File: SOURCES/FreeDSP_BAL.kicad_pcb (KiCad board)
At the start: 2 copper layers, 100 x 100 mm, 187 parts, among them IC1 AD8608ARZ, IC2 ADAU1701, IC3 24AA256, IC4 SN74LVC1G08DBVR, IC5 AD8608ARZ, IC6 AD8608ARZ, IC7 74HC4040D, P10 CONN_02X10, P11 MM-16G, P12 MM-12G, P2 BARREL_JACK, P3 CONN_02X02, P4 USBi, P5 CONN_02X13, P6 CONN_01X06, P7 CONN_01X06, P8 CONN_01X06, P9 CONN_02X10, Q1 ZXTP25040DFHTA, Q2 2N7000, Q3 2N7000, U1 78033, U3 7805

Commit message: Correction of some typos
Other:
- board text added: "12V->exp"
- board text removed: "exp 5V"
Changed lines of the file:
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@@
     (links 416)
     (no_connects 0)
-    (area 99.949999 49.949999 200.050001 150.050001)
+    (area 93.224999 49.949999 202.475621 150.050001)
     (thickness 1.6)
     (drawings 13)
@@
     (pad 17 thru_hole circle (at 8.385 0.53 270) (size 1.5 1.5) (drill 1.5) (layers *.Cu *.Mask F.SilkS))
   )
-  (gr_text "Designed in Germany" (at 168.9 147.3) (layer F.SilkS)
+  (gr_text "Designed in Germany" (at 150.2 134.6 90) (layer F.SilkS)
     (effects (font (size 1.5 1.5) (thickness 0.3)))
   )
-  (gr_text freeDSP-CLASSIC-BAL-A (at 193 124 90) (layer F.SilkS)
+  (gr_text freeDSP-CLASSIC-BAL-A (at 147.5 132 90) (layer F.SilkS)
     (effects (font (size 1.5 1.5) (thickness 0.3)))
   )
@@
   (gr_line (start 100 50) (end 200 50) (layer Edge.Cuts) (width 0.1))
   (gr_line (start 100 150) (end 100 50) (layer Edge.Cuts) (width 0.1))
-  (gr_text "exp 5V" (at 184.5 76.5 90) (layer F.SilkS)
+  (gr_text 12V->exp (at 184.1 77.9 90) (layer F.SilkS)
     (effects (font (size 1.5 1.5) (thickness 0.3)))
   )

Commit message: Changed expansion header to 2.54 IDC
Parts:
- OSC1: value 12M288Hz -> 24M576Hz
- P11: footprint rklib:MM-16G -> Connect:IDC_Header_Straight_16pins
- R22, R23: value 680R -> 6K04
- R26, R27: value 47K0 -> 49K9
- R7, R8: value 604R -> 6K04
- moved P11 11.5 mm to (196.5, 92.1), turned to 90 degrees
- moved P12 5.50 mm to (195.5, 106.6)
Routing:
- net _RESET: track 72.5 -> 64.2 mm
- net MP9: track 30.1 -> 36.1 mm
- net MP8: track 32.6 -> 37.9 mm
- net +5V: track 329.4 -> 324.1 mm
- net MP3: track 32.6 -> 37.9 mm
- net SDA: track 112.5 -> 107.8 mm
- net MP2: track 36.8 -> 41.1 mm
- net SCL: track 107.3 -> 103.5 mm
- net MP7: track 25.0 -> 28.2 mm
- net MP1: track 31.6 -> 28.9 mm
- net MP5: track 34.0 -> 31.4 mm
- net MDO: track 36.2 -> 34.8 mm
- net MDI: track 45.5 -> 44.1 mm
- net MP4: track 32.0 -> 30.8 mm
- net Net-(JP1-Pad1): track 35.4 -> 36.3 mm
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
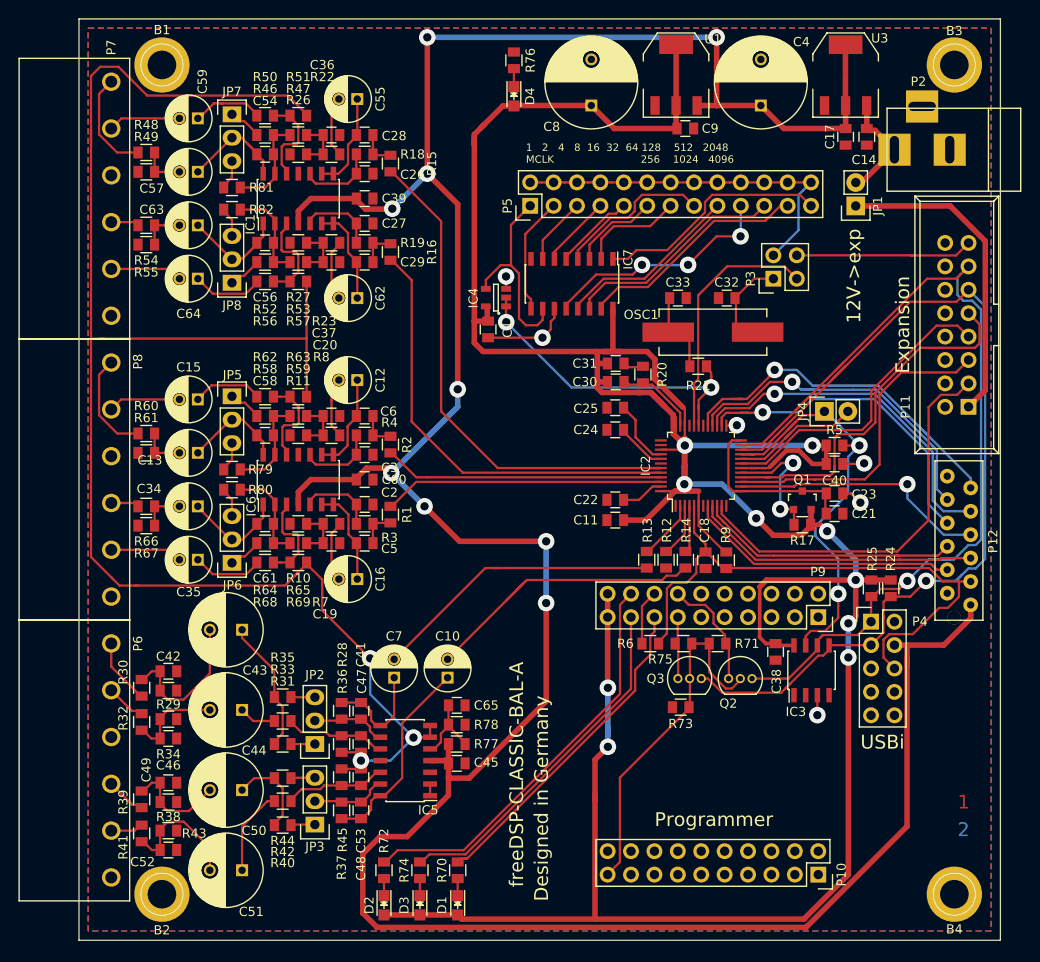
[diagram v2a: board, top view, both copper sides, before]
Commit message: Revision C: Improvement of input and output stages. Added some fault protection.
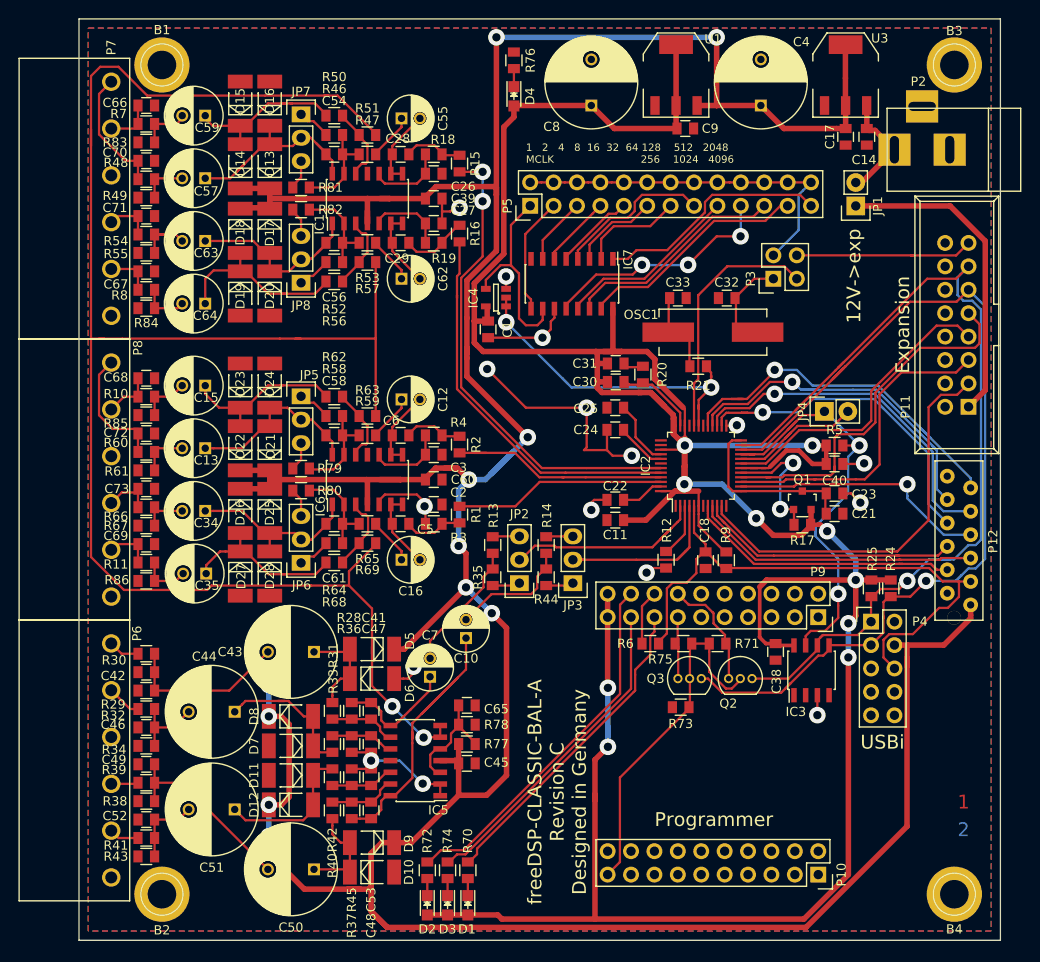
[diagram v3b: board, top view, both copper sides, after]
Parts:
- removed C19, C20, C36, C37: 3n30, rklib:C0805-X7R
- removed R22, R23: 6K04, rklib:C0805-RES
- removed R26, R27: 49K9, rklib:C0805-RES
- added C66: 2n20, rklib:C0805-X7R, F.Cu at (107.3, 59.4)
- added C67: 2n20, rklib:C0805-X7R, F.Cu at (107.3, 77.4)
- added C68: 2n20, rklib:C0805-X7R, F.Cu at (107.3, 89.0)
- added C69: 2n20, rklib:C0805-X7R, F.Cu at (107.3, 107.0)
- added C70: 2n20, rklib:C0805-X7R, F.Cu at (107.3, 65.4)
- added C71: 2n20, rklib:C0805-X7R, F.Cu at (107.3, 71.4)
- added C72: 2n20, rklib:C0805-X7R, F.Cu at (107.3, 95.0)
- added C73: 2n20, rklib:C0805-X7R, F.Cu at (107.3, 101.0)
- added D10: LL4002, Diodes_SMD:MELF_Standard, F.Cu at (131.8, 142.6)
- added D11: LL4002, Diodes_SMD:MELF_Standard, F.Cu at (123.0, 132.1)
- added D12: LL4002, Diodes_SMD:MELF_Standard, F.Cu at (123.0, 135.3)
- added D13: LL4002, Diodes_SMD:MELF_Standard, F.Cu at (120.7, 66.0)
- added D14: LL4002, Diodes_SMD:MELF_Standard, F.Cu at (117.5, 66.0)
- added D15: LL4002, Diodes_SMD:MELF_Standard, F.Cu at (117.5, 59.2)
- added D16: LL4002, Diodes_SMD:MELF_Standard, F.Cu at (120.7, 59.2)
- added D17: LL4002, Diodes_SMD:MELF_Standard, F.Cu at (120.7, 73.0)
- added D18: LL4002, Diodes_SMD:MELF_Standard, F.Cu at (117.5, 73.0)
- added D19: LL4002, Diodes_SMD:MELF_Standard, F.Cu at (117.5, 79.8)
- added D20: LL4002, Diodes_SMD:MELF_Standard, F.Cu at (120.7, 79.8)
- added D21: LL4002, Diodes_SMD:MELF_Standard, F.Cu at (120.7, 96.6)
- added D22: LL4002, Diodes_SMD:MELF_Standard, F.Cu at (117.5, 96.6)
- added D23: LL4002, Diodes_SMD:MELF_Standard, F.Cu at (117.5, 89.8)
- added D24: LL4002, Diodes_SMD:MELF_Standard, F.Cu at (120.7, 89.8)
- added D25: LL4002, Diodes_SMD:MELF_Standard, F.Cu at (120.7, 103.4)
- added D26: LL4002, Diodes_SMD:MELF_Standard, F.Cu at (117.5, 103.4)
- added D27: LL4002, Diodes_SMD:MELF_Standard, F.Cu at (117.5, 110.2)
- added D28: LL4002, Diodes_SMD:MELF_Standard, F.Cu at (120.7, 110.2)
- added D5: LL4002, Diodes_SMD:MELF_Standard, F.Cu at (131.8, 118.4)
- added D6: LL4002, Diodes_SMD:MELF_Standard, F.Cu at (131.8, 121.6)
- added D7: LL4002, Diodes_SMD:MELF_Standard, F.Cu at (123.0, 128.9)
- added D8: LL4002, Diodes_SMD:MELF_Standard, F.Cu at (123.0, 125.7)
- added D9: LL4002, Diodes_SMD:MELF_Standard, F.Cu at (131.8, 139.4)
- added R83: 100K, rklib:C0805-RES, F.Cu at (107.3, 63.4)
- added R84: 100K, rklib:C0805-RES, F.Cu at (107.3, 81.4)
- added R85: 100K, rklib:C0805-RES, F.Cu at (107.3, 93.0)
- added R86: 100K, rklib:C0805-RES, F.Cu at (107.3, 111.0)
- C10, C12, C16, C55, C62, C7: value 47u0./16V -> 100u./16V
- C13, C15, C34, C35, C57, C59, C63, C64: value 47u0./16V -> 47u0./50V; footprint Capacitors_ThroughHole:C_Radial_D5_L11_P2 -> Capacitors_ThroughHole:C_Radial_D6.3_L11.2_P2.5
- C43, C44, C50, C51: value 47u0./35V -> 47u0./63V; footprint Capacitors_ThroughHole:C_Radial_D8_L11.5_P3.5 -> Capacitors_ThroughHole:C_Radial_D10_L16_P5
- C65: value 100n -> 22u0./X5R
- P11: value MM-16G -> IDC-16G
- R10, R11: value 49K9 -> 56R0
- R13, R14: value 7K15 -> 9K09
- R31, R33, R40, R42: value 17K4 -> 14K0
- R35, R44: value 3K57 -> 261R
- R7, R8: value 6K04 -> 56R0
- moved R7 47.8 mm to (107.3, 61.4), turned to 0 degrees
- moved JP3 38.3 mm to (153.6, 111.2)
- moved R44 36.0 mm to (150.7, 110.6), turned to 90 degrees
- moved JP2 28.2 mm to (147.8, 111.2)
- moved R35 26.2 mm to (144.9, 110.6), turned to 90 degrees
- moved R8 25.6 mm to (107.3, 79.4), turned to 0 degrees
- moved R10 21.5 mm to (107.3, 91.0), turned to 0 degrees
- moved R11 21.5 mm to (107.3, 109.0), turned to 0 degrees
- moved R13 16.8 mm to (144.9, 107.1)
- moved R14 15.2 mm to (150.7, 107.1)
- moved C50 11.6 mm to (125.5, 142.3)
- moved C43 8.16 mm to (125.5, 118.7)
- moved R53 7.79 mm to (131.3, 74.3)
- moved R59 7.79 mm to (131.3, 95.2)
- moved R65 7.79 mm to (131.3, 104.8)
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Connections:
- net /DAC0 renamed /DAC4
- C15 pad 2: /OUT3- -> Net-(C15-Pad2)
- C35 pad 2: /OUT4- -> Net-(C35-Pad2)
- C47 pad 2: /Vcom -> /VO1
- C5 pad 1: Net-(C16-Pad1) -> Net-(C16-Pad2)
- C53 pad 2: /Vcom -> /VO1
- C55 pad 1: Net-(C28-Pad1) -> Net-(C55-Pad1)
- C55 pad 2: Net-(C55-Pad2) -> Net-(C28-Pad1)
- C59 pad 2: /OUT1- -> Net-(C59-Pad2)
- C6 pad 1: Net-(C12-Pad1) -> Net-(C12-Pad2)
- C62 pad 1: Net-(C29-Pad1) -> Net-(C62-Pad1)
- C62 pad 2: Net-(C62-Pad2) -> Net-(C29-Pad1)
- C64 pad 2: /OUT2- -> Net-(C64-Pad2)
- IC2 pad 44: /DAC1 -> /DAC3
- IC2 pad 46: /DAC3 -> /DAC1
- IC5 pad 1: Net-(IC5-Pad1) -> /VO1
- IC5 pad 2: Net-(IC5-Pad1) -> /VO1
- IC5 pad 3: GND -> Net-(C65-Pad2)
- IC5 pad 6: /Vcom -> /VO2
- IC5 pad 7: /Vcom -> /VO2
- IC6 pad 6: Net-(C16-Pad1) -> Net-(C16-Pad2)
- IC6 pad 7: Net-(C16-Pad1) -> Net-(C16-Pad2)
- IC6 pad 8: Net-(C12-Pad1) -> Net-(C12-Pad2)
- IC6 pad 9: Net-(C12-Pad1) -> Net-(C12-Pad2)
- JP2 pad 2: Net-(C41-Pad2) -> /IN1
- JP3 pad 2: Net-(C48-Pad2) -> /IN2
- R1 pad 2: /DAC3 -> /DAC1
- R10 pad 1: /OUT4 -> /OUT3-
- R10 pad 2: GND -> Net-(C15-Pad2)
- R11 pad 1: /OUT3 -> /OUT4-
- R11 pad 2: GND -> Net-(C35-Pad2)
- R13 pad 2: /IN1 -> Net-(JP2-Pad3)
- R14 pad 2: /IN2 -> Net-(JP3-Pad3)
- R16 pad 2: /DAC1 -> /DAC3
- R31 pad 1: Net-(JP2-Pad1) -> Net-(C41-Pad2)
- R35 pad 1: Net-(JP2-Pad3) -> Net-(JP2-Pad1)
- R35 pad 2: Net-(C43-Pad1) -> Net-(C7-Pad2)
- R36 pad 2: /Vcom -> /VO1
- R40 pad 1: Net-(JP3-Pad1) -> Net-(C48-Pad2)
- R44 pad 1: Net-(JP3-Pad3) -> Net-(JP3-Pad1)
- R44 pad 2: Net-(C50-Pad1) -> Net-(C10-Pad2)
- R45 pad 2: /Vcom -> /VO1
- R47 pad 2: /OUT1 -> Net-(C55-Pad1)
- R51 pad 2: /Vcom -> /VO2
- R53 pad 2: /OUT2 -> Net-(C62-Pad1)
- R57 pad 2: /Vcom -> /VO2
- R59 pad 2: /OUT3 -> Net-(C12-Pad1)
- R63 pad 1: /Vcom -> /VO2
- R65 pad 2: /OUT4 -> Net-(C16-Pad1)
- R69 pad 2: /Vcom -> /VO2
- R7 pad 1: Net-(C16-Pad2) -> /OUT1-
- R7 pad 2: /OUT4 -> Net-(C59-Pad2)
- R8 pad 1: Net-(C12-Pad2) -> /OUT2-
- R8 pad 2: /OUT3 -> Net-(C64-Pad2)
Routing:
- net /VO2: track 0.00 -> 197.6 mm, vias 0 -> 2
- net /Vcom: track 183.8 -> 0.00 mm, vias 3 -> 0
- net +5V: track 324.1 -> 410.8 mm, vias 9 -> 11
- net GND: track 33.5 -> 71.1 mm, vias 6 -> 13
- net /DAC1: track 47.9 -> 23.1 mm
- net Net-(C10-Pad2): track 33.8 -> 13.4 mm
- net Net-(C7-Pad2): track 31.9 -> 14.3 mm
- net /IN1: track 6.54 -> 22.6 mm
- net /VO1: track 0.00 -> 15.8 mm, vias 0 -> 2
- net /IN2: track 5.13 -> 20.3 mm
- net Net-(C64-Pad1): track 7.71 -> 21.6 mm
- net /DAC3: track 30.4 -> 42.4 mm
- net Net-(C44-Pad1): track 4.10 -> 16.0 mm
- net Net-(C35-Pad1): track 7.59 -> 18.7 mm
- net Net-(C15-Pad1): track 7.66 -> 18.4 mm
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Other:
- board text added: "freeDSP-CLASSIC-BAL-A Revision C Designed in Germany"
- board text removed: "Designed in Germany"
- board text removed: "freeDSP-CLASSIC-BAL-A"
